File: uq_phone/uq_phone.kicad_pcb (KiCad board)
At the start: 4 copper layers, 116.9 x 105 mm, 169 parts, among them J1 USB4105-GF-A, J10 Conn_01x02, J11 FTSH-105-XX-X-DV, J2 S3B-PH-SM4-TB_LF__SN_, J3 20279-001E-03, J4 20279-001E-03, J5 KP15B-6S-SF_800_, J7 Conn_01x02, J8 541324562, J9 SJ-3551B-MSMT-TR-67, Q1 MMBT3904, Q2 MMBT3904, U1 MCP73871-2CCI_ML, U10 TS3A5018RSVR, U11 NAU88C22YG, U12 MCP1664T-E/OT, U13 TPD3F303DQDR, U14 TPD8F003DQDR, U2 TPS62162DSGR, U3 BQ27441DRZR-G1A, U4 RC7620_1104625, U5 TXB0108RGYR, U6 TXB0108RGYR, U7 STM32H730VBTx, U8 LSM6DSVTR, U9 DRV2603RUNR

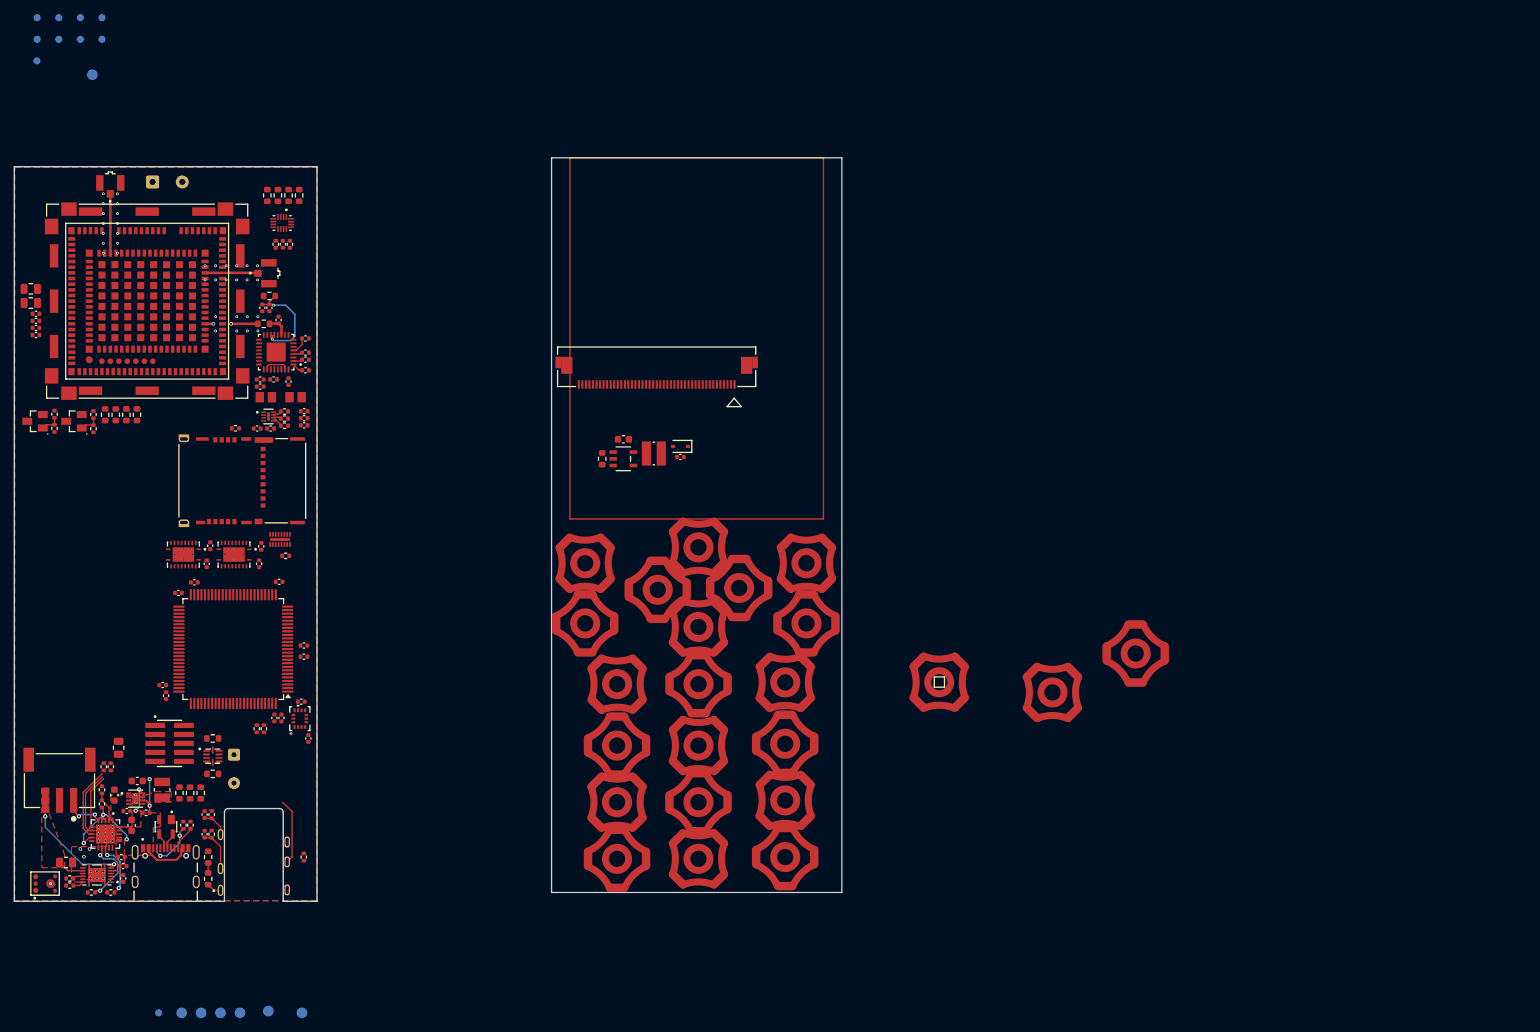
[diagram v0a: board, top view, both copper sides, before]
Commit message: Add LEDs, Inital Buttons
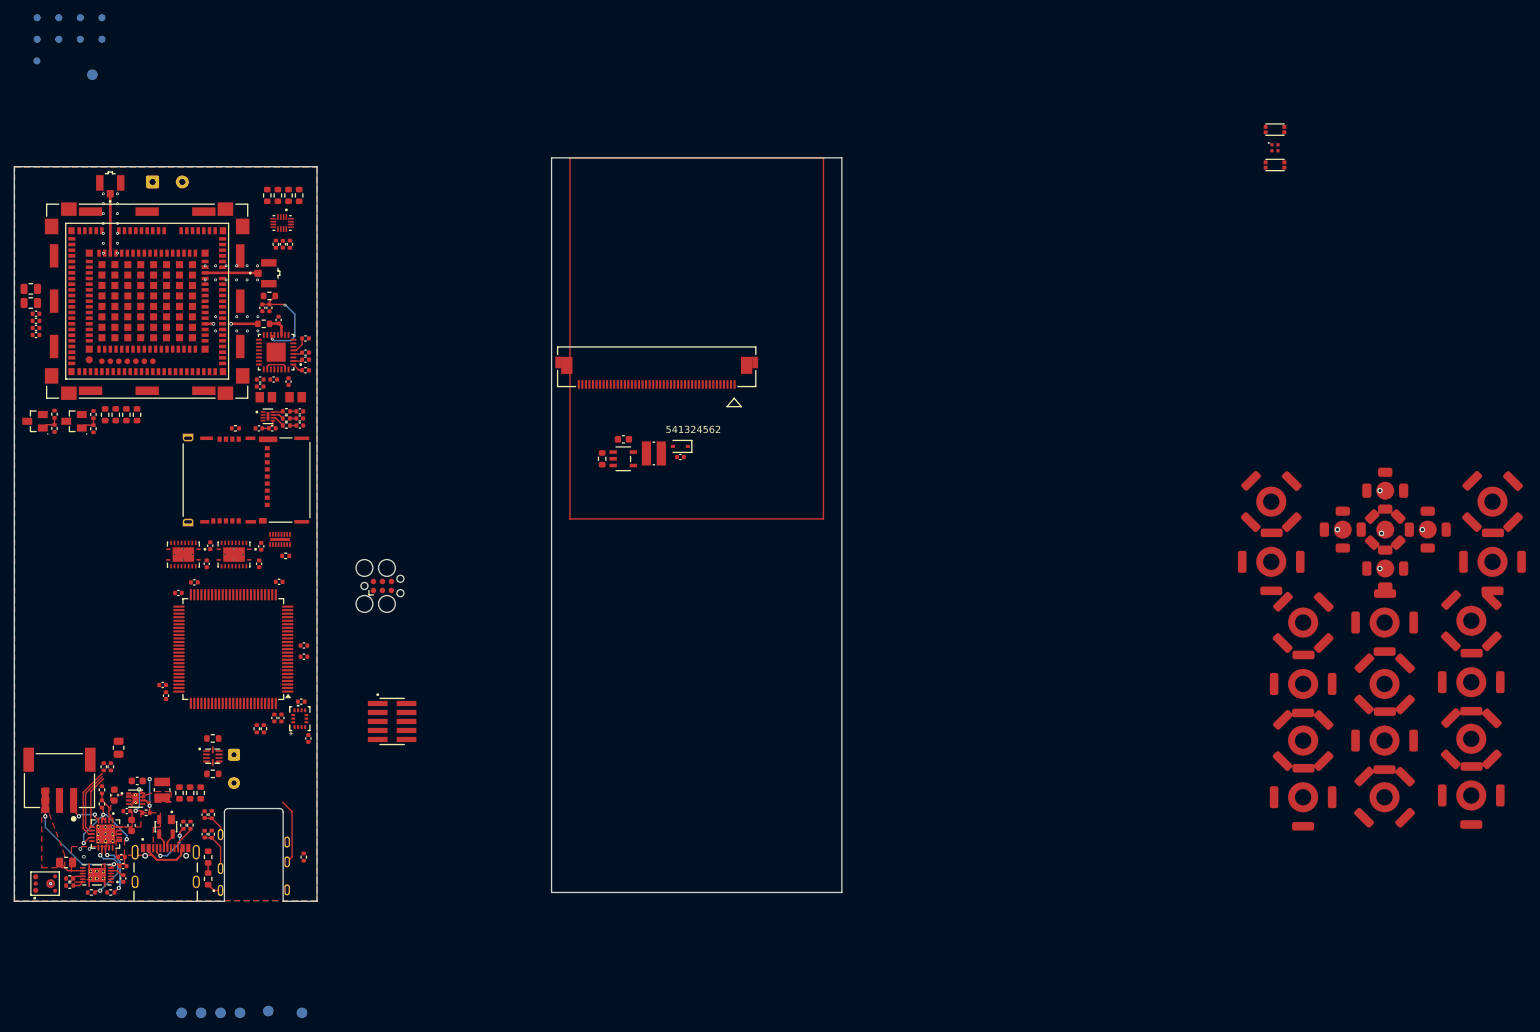
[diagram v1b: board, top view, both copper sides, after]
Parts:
- removed the REF** at (124.0, 133.2)
- removed the REF** at (118.2, 128.0)
- removed the REF** at (124.0, 122.0)
- removed the REF** at (185.8, 137.0)
- removed the REF** at (158.0, 141.1)
- removed the REF** at (174.0, 142.5)
- removed the REF** at (129.8, 127.8)
- removed TP19: TestPoint, TestPoint:TestPoint_Pad_D1.0mm
- removed U13: TPD3F303DQDR, TPD3F303DQDR:SON40P170X135X80-9N
- added J12: Conn_ARM_SWD_TagConnect_TC2030, Connector:Tag-Connect_TC2030-IDC-FP_2x03_P1.27mm_Vertical, F.Cu at (79.4, 127.5)
- added LED1: XINGLIGHT XL-1010RGBC-WS2812B, custom_footprints:XL-1010RGBC-WS2812B, F.Cu at (205.0, 65.2)
- added REF**: 6mmSnaptron, custom_footprints:6mmSnaptron, F.Cu at (215.0, 119.5)
- added REF**: 6mmSnaptron, custom_footprints:6mmSnaptron, F.Cu at (221.0, 114.0)
- added REF**: 6mmSnaptron, custom_footprints:6mmSnaptron, F.Cu at (221.0, 119.5)
- added REF**: 6mmSnaptron, custom_footprints:6mmSnaptron, F.Cu at (227.0, 119.5)
- added REF**: 6mmSnaptron, custom_footprints:6mmSnaptron, F.Cu at (221.0, 125.0)
- added SW1: SKTAAAE010, custom_footprints:SKTAAAE010, F.Cu at (204.1, 62.6)
- added SW2: SKTAAAE010, custom_footprints:SKTAAAE010, F.Cu at (204.1, 67.6)
- added U10: TPD3F303DQDR, TPD3F303DQDR:SON40P170X135X80-9N, F.Cu at (63.2, 103.5)
- moved REF** 97.3 mm to (236.2, 115.5)
- moved REF** 97.3 mm to (209.4, 149.3)
- moved REF** 97.3 mm to (209.4, 157.3)
- moved REF** 97.3 mm to (209.4, 141.3)
- moved REF** 97.3 mm to (220.9, 149.3)
- moved REF** 97.3 mm to (204.9, 124.0)
- moved REF** 97.3 mm to (204.9, 115.5)
- moved REF** 97.3 mm to (220.9, 157.3)
- moved REF** 97.3 mm to (220.9, 141.3)
- moved REF** 97.3 mm to (233.2, 157.1)
- moved REF** 97.3 mm to (233.2, 141.1)
- moved REF** 97.3 mm to (236.2, 124.0)
- moved REF** 97.3 mm to (233.2, 149.1)
- moved REF** 97.3 mm to (209.4, 132.6)
- moved REF** 97.3 mm to (220.9, 132.6)
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- renumbered C34 to C50, C46 to C56, MK1 to MK2, U10 to U15, U11 to U16
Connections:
- C39 pad 1: Net-(U11-RMICN) -> unconnected-(C39-Pad1)
- C44 pad 1: Net-(U11-VREF) -> unconnected-(C44-Pad1)
- C56 pad 1: Net-(MK1-OUTPUT) -> (no net)
- MK2 pad 1: Net-(MK1-OUTPUT) -> (no net)
- R41 pad 2: Net-(U10-~{EN}) -> unconnected-(R41-Pad2)
- U15 pad 13: Net-(U10-~{EN}) -> unconnected-(R41-Pad2)
- U16 pad 19: unconnected-(U11-LAUXIN-Pad19) -> (no net)
- U16 pad 20: unconnected-(U11-RAUXIN-Pad20) -> (no net)
- U16 pad 21: unconnected-(U11-AUXOUT1-Pad21) -> (no net)
- U16 pad 22: unconnected-(U11-AUXOUT2-Pad22) -> (no net)
- U16 pad 27: Net-(U11-VREF) -> unconnected-(C44-Pad1)
- U16 pad 3: unconnected-(U11-LLIN/GPIO2-Pad3) -> (no net)
- U16 pad 5: Net-(U11-RMICN) -> unconnected-(C39-Pad1)
- U16 pad 6: unconnected-(U11-RLIN/GPIO3-Pad6) -> (no net)
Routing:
- net unconnected-(C39-Pad1): track 0.00 -> 2.44 mm
- net Net-(U11-RMICN): track 2.44 -> 0.00 mm
- net SIM_VDD: track 0.00 -> 2.26 mm
- net SIM_RST: track 0.00 -> 0.91 mm
- net SIM_DATA: track 0.00 -> 0.91 mm
- net SIM_CLK: track 0.00 -> 0.90 mm

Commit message: Routing Init
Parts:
- removed the J11 at (80.7, 146.6)
- removed the REF** at (209.4, 132.6)
- removed the REF** at (236.2, 115.5)
- removed the REF** at (209.4, 149.3)
- removed the REF** at (209.4, 157.3)
- removed the REF** at (209.4, 141.3)
- removed the REF** at (220.9, 149.3)
- removed the REF** at (204.9, 124.0)
- removed the REF** at (215.0, 119.5)
- removed the REF** at (221.0, 114.0)
- removed the REF** at (204.9, 115.5)
- removed the REF** at (220.9, 157.3)
- removed the REF** at (220.9, 141.3)
- removed the REF** at (221.0, 119.5)
- removed the REF** at (233.2, 157.1)
- removed the REF** at (227.0, 119.5)
- removed the REF** at (220.9, 132.6)
- removed the REF** at (233.2, 141.1)
- removed the REF** at (233.2, 132.4)
- removed the REF** at (236.2, 124.0)
- removed the REF** at (233.2, 149.1)
- removed the REF** at (221.0, 125.0)
- removed SW1, SW2: SKTAAAE010, custom_footprints:SKTAAAE010
- added LED10: XL-1010RGBC, custom_footprints:XL-1010RGBC-WS2812B, F.Cu at (115.4, 139.4)
- added LED11: XL-1010RGBC, custom_footprints:XL-1010RGBC-WS2812B, F.Cu at (115.4, 141.9)
- added LED12: XL-1010RGBC, custom_footprints:XL-1010RGBC-WS2812B, F.Cu at (115.4, 144.5)
- added LED13: XL-1010RGBC, custom_footprints:XL-1010RGBC-WS2812B, F.Cu at (118.2, 131.8)
- added LED14: XL-1010RGBC, custom_footprints:XL-1010RGBC-WS2812B, F.Cu at (118.2, 134.4)
- added LED15: XL-1010RGBC, custom_footprints:XL-1010RGBC-WS2812B, F.Cu at (118.2, 136.9)
- added LED16: XL-1010RGBC, custom_footprints:XL-1010RGBC-WS2812B, F.Cu at (118.2, 139.4)
- added LED17: XL-1010RGBC, custom_footprints:XL-1010RGBC-WS2812B, F.Cu at (118.2, 141.9)
- added LED2: XL-1010RGBC, custom_footprints:XL-1010RGBC-WS2812B, F.Cu at (112.7, 134.4)
- added LED3: XL-1010RGBC, custom_footprints:XL-1010RGBC-WS2812B, F.Cu at (112.7, 136.9)
- added LED4: XL-1010RGBC, custom_footprints:XL-1010RGBC-WS2812B, F.Cu at (112.7, 139.4)
- added LED5: XL-1010RGBC, custom_footprints:XL-1010RGBC-WS2812B, F.Cu at (112.7, 141.9)
- added LED6: XL-1010RGBC, custom_footprints:XL-1010RGBC-WS2812B, F.Cu at (112.7, 144.5)
- added LED7: XL-1010RGBC, custom_footprints:XL-1010RGBC-WS2812B, F.Cu at (115.4, 131.8)
- added LED8: XL-1010RGBC, custom_footprints:XL-1010RGBC-WS2812B, F.Cu at (115.4, 134.4)
- added LED9: XL-1010RGBC, custom_footprints:XL-1010RGBC-WS2812B, F.Cu at (115.4, 136.9)
- added R48: 330R, Resistor_SMD:R_0402_1005Metric, F.Cu at (108.8, 145.3)
- added REF**: 8.5mmSnaptron, custom_footprints:8.5mmSnaptron, F.Cu at (220.4, 151.7)
- added REF**: 8.5mmSnaptron, custom_footprints:8.5mmSnaptron, F.Cu at (232.7, 159.4)
- added REF**: 8.5mmSnaptron, custom_footprints:8.5mmSnaptron, F.Cu at (235.7, 118.0)
- added REF**: 8.5mmSnaptron, custom_footprints:8.5mmSnaptron, F.Cu at (232.7, 143.4)
- added REF**: 8.5mmSnaptron, custom_footprints:8.5mmSnaptron, F.Cu at (208.9, 151.7)
- added REF**: 8.5mmSnaptron, custom_footprints:8.5mmSnaptron, F.Cu at (204.4, 118.0)
- added REF**: 8.5mmSnaptron, custom_footprints:8.5mmSnaptron, F.Cu at (232.7, 151.4)
- added REF**: 6mmSnaptron, custom_footprints:6mmSnaptron, F.Cu at (220.5, 127.4)
- added REF**: 8.5mmSnaptron, custom_footprints:8.5mmSnaptron, F.Cu at (220.4, 135.0)
- added REF**: 6mmSnaptron, custom_footprints:6mmSnaptron, F.Cu at (226.5, 121.9)
- added REF**: 6mmSnaptron, custom_footprints:6mmSnaptron, F.Cu at (214.5, 121.9)
- added REF**: 8.5mmSnaptron, custom_footprints:8.5mmSnaptron, F.Cu at (204.4, 126.5)
- added REF**: 6mmSnaptron, custom_footprints:6mmSnaptron, F.Cu at (220.5, 116.4)
- added REF**: 8.5mmSnaptron, custom_footprints:8.5mmSnaptron, F.Cu at (208.9, 135.0)
- added REF**: 8.5mmSnaptron, custom_footprints:8.5mmSnaptron, F.Cu at (220.4, 159.7)
- added REF**: 6mmSnaptron, custom_footprints:6mmSnaptron, F.Cu at (220.5, 121.9)
- added REF**: 8.5mmSnaptron, custom_footprints:8.5mmSnaptron, F.Cu at (220.4, 143.7)
- added REF**: 8.5mmSnaptron, custom_footprints:8.5mmSnaptron, F.Cu at (232.7, 134.8)
- added REF**: 8.5mmSnaptron, custom_footprints:8.5mmSnaptron, F.Cu at (208.9, 143.7)
- added REF**: 8.5mmSnaptron, custom_footprints:8.5mmSnaptron, F.Cu at (208.9, 159.7)
- added REF**: 8.5mmSnaptron, custom_footprints:8.5mmSnaptron, F.Cu at (235.7, 126.5)
- LED1: value XINGLIGHT XL-1010RGBC-WS2812B -> XL-1010RGBC
- Q1, Q2: value MMBT3904 -> MMBT3904LP-7; footprint MMBT3904LT1G:SOT95P240X111-3N -> MMBT3904LP-7:DFN101X61X53-3N
- moved LED1 113.9 mm to (112.7, 131.8)
- moved TP6 111.9 mm to (29.7, 82.6)
- moved C27 51.0 mm to (49.2, 102.0), turned to 180 degrees
- moved C28 46.6 mm to (47.4, 102.0), turned to 0 degrees
- moved TP10 46.5 mm to (40.2, 93.5)
- moved U8 46.4 mm to (48.3, 104.1), turned to 180 degrees
- moved R45 46.3 mm to (61.7, 119.9), turned to 180 degrees
- moved TP12 44.8 mm to (42.3, 93.5)
- moved TP11 44.5 mm to (41.2, 91.7)
- moved TP14 44.0 mm to (44.3, 93.5)
- moved TP16 43.3 mm to (46.4, 93.6)
- moved TP2 42.7 mm to (28.8, 157.8)
- moved TP13 42.6 mm to (43.4, 91.8)
- moved TP15 42.0 mm to (45.4, 91.8)
- moved TP9 40.3 mm to (35.7, 87.4)
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- renumbered C15 to C10, C16 to C11, C17 to C12, C18 to C13, C19 to C14, C20 to C15, C21 to C16, C22 to C17, C23 to C18, C24 to C19, C25 to C20, C26 to C21, C27 to C22, C28 to C23, C29 to C24, C30 to C25, C31 to C26, C32 to C27, C33 to C28, C8 to C29, C9 to C30, C10 to C31, C11 to C32, C12 to C33, C48 to C34, C49 to C35, C50 to C36, C35 to C37, C36 to C38, C37 to C39, C38 to C40, C39 to C41, C56 to C42, C47 to C43, C40 to C44, C41 to C45, C42 to C46, C43 to C47, C44 to C48, C45 to C49, C7 to C6, C6 to C7, C13 to C8, C14 to C9, D5 to D2, J9 to J10, J10 to J11, J12 to J6, J5 to J8, J8 to J9, MK2 to MK1, R8 to R10, R39 to R23, R26 to R24, R27 to R25, R28 to R26, R29 to R27, R30 to R28, R31 to R29, R23 to R30, R24 to R31, R25 to R32, R32 to R33, R38 to R34, R40 to R35, R41 to R36, R42 to R37, R47 to R38, R48 to R39, R43 to R40, R44 to R41, R45 to R42, R46 to R43, R49 to R44, R50 to R45, R51 to R46, R54 to R47, R9 to R8, R10 to R9, U14 to U11, U15 to U13, U16 to U14
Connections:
- C41 pad 1: unconnected-(C39-Pad1) -> Net-(U14-RMICN)
- C42 pad 1: (no net) -> Net-(MK1-OUTPUT)
- C48 pad 1: unconnected-(C44-Pad1) -> Net-(U14-VREF)
- D1 pad 3: USB_P -> USB_N
- D1 pad 4: USB_N -> USB_P
- LED1 pad 1: unconnected-(LED1-DO-Pad1) -> Net-(LED1-DO)
- LED1 pad 2: unconnected-(LED1-VDD-Pad2) -> +3.3V
- LED1 pad 3: unconnected-(LED1-GND-Pad3) -> GND
- LED1 pad 4: unconnected-(LED1-DI-Pad4) -> Net-(LED1-DI)
- MK1 pad 1: (no net) -> Net-(MK1-OUTPUT)
- R35 pad 1: AUD_SW -> AUD_SW_L
- R36 pad 2: unconnected-(R41-Pad2) -> Net-(U13-~{EN})
- U13 pad 13: unconnected-(R41-Pad2) -> Net-(U13-~{EN})
- U13 pad 15: AUD_SW -> AUD_SW_L
- U13 pad 9: MCU_AUD_IN -> unconnected-(U13-NC3-Pad9)
- U14 pad 19: (no net) -> unconnected-(U14-LAUXIN-Pad19)
- U14 pad 20: (no net) -> unconnected-(U14-RAUXIN-Pad20)
- U14 pad 21: (no net) -> unconnected-(U14-AUXOUT1-Pad21)
- U14 pad 22: (no net) -> unconnected-(U14-AUXOUT2-Pad22)
- U14 pad 27: unconnected-(C44-Pad1) -> Net-(U14-VREF)
- U14 pad 3: (no net) -> unconnected-(U14-LLIN/GPIO2-Pad3)
- U14 pad 5: unconnected-(C39-Pad1) -> Net-(U14-RMICN)
- U14 pad 6: (no net) -> unconnected-(U14-RLIN/GPIO3-Pad6)
- U4 pad 38: MOB_GNSS_ANT -> unconnected-(U4A-RF_GNSS-Pad38)
- U4 pad P1: (no net) -> GND
- U4 pad P10: (no net) -> GND
- U4 pad P11: (no net) -> GND
- U4 pad P12: (no net) -> GND
- U4 pad P13: (no net) -> GND
- U4 pad P14: (no net) -> GND
- U4 pad P15: (no net) -> GND
- U4 pad P16: (no net) -> GND
- U4 pad P17: (no net) -> GND
- U4 pad P18: (no net) -> GND
- U4 pad P19: (no net) -> GND
- U4 pad P2: (no net) -> GND
- U4 pad P20: (no net) -> GND
- U4 pad P3: (no net) -> GND
- U4 pad P4: (no net) -> GND
- U4 pad P5: (no net) -> GND
- U4 pad P6: (no net) -> GND
- U4 pad P7: (no net) -> GND
- U4 pad P8: (no net) -> GND
- U4 pad P9: (no net) -> GND
- U5 pad 1: MOB_DTR -> MOB_DSR
- U5 pad 12: MCU_DSR -> MCU_RI
- U5 pad 16: MCU_RI -> MCU_RXD
- U5 pad 17: MCU_DCD -> MCU_DTR
- U5 pad 18: MCU_RXD -> MCU_DCD
- U5 pad 20: MCU_DTR -> MCU_DSR
- U5 pad 3: MOB_RXD -> MOB_DCD
- U5 pad 4: MOB_DCD -> MOB_DTR
- U5 pad 5: MOB_RI -> MOB_RXD
- U5 pad 9: MOB_DSR -> MOB_RI
- U6 pad 12: AUD_SW_H -> MCU_AUD_OUT_L_H
- U6 pad 13: MCU_AUD_SYNC_H -> MCU_AUD_BCLK_H
- U6 pad 14: MCU_AUD_BCLK_H -> AUD_SW_H
- U6 pad 15: MCU_AUD_OUT_L_H -> MCU_AUD_SYNC_H
- U6 pad 6: MCU_AUD_OUT_L -> MCU_AUD_SYNC_L
- U6 pad 7: MCU_AUD_BCLK_L -> AUD_SW_L
- U6 pad 8: MCU_AUD_SYNC_L -> MCU_AUD_BCLK_L
- U6 pad 9: AUD_SW_L -> MCU_AUD_OUT_L
- U7 pad 35: unconnected-(U7-PB1-Pad35) -> MOB_WAKE_H
- U7 pad 36: unconnected-(U7-PB2-Pad36) -> MOB_PWR_CTL
- U7 pad 47: unconnected-(U7-PB11-Pad47) -> MOB_RST_CTL
- U7 pad 59: MCU_DTR -> MCU_DCD
- U7 pad 60: MCU_DCD -> MCU_DTR
- U7 pad 91: MOB_RST_CTL -> unconnected-(U7-PB5-Pad91)
- U7 pad 92: MOB_WAKE_H -> unconnected-(U7-PB6-Pad92)
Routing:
- net +1.8V: track 0.00 -> 112.0 mm, vias 0 -> 6
- net Net-(MK1-OUTPUT): track 0.00 -> 110.4 mm, vias 0 -> 2
- net +3.3V: track 6.14 -> 111.2 mm, vias 2 -> 7
- net AGND: track 0.00 -> 99.7 mm, vias 0 -> 3
- net HP_DET: track 9.27 -> 90.3 mm, vias 0 -> 5
- net Net-(C37-Pad2): track 1.43 -> 81.5 mm, vias 0 -> 2
- net +VMOB: track 0.00 -> 80.0 mm, vias 0 -> 1
- net SDA: track 0.00 -> 64.0 mm, vias 0 -> 4
- net SCL: track 0.00 -> 63.4 mm, vias 0 -> 4
- net Net-(U4A-USB_VBUS): track 0.00 -> 63.0 mm, vias 0 -> 2
- net /Mobile/MOB_USB_N: track 0.00 -> 63.0 mm, vias 0 -> 2
- net /Mobile/MOB_USB_P: track 0.00 -> 62.9 mm, vias 0 -> 2
- net FUEL_GPO: track 1.56 -> 56.6 mm, vias 0 -> 3
- net MCU_AUD_SYNC_L: track 0.00 -> 53.1 mm, vias 0 -> 2
- net MCU_AUD_BCLK_L: track 0.00 -> 53.1 mm, vias 0 -> 2
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- added copper zone on F.Cu, net +VMOB
- added copper zone on B.Cu, net AGND
- added copper zone on F.Cu, net AGND
- added copper zone on In2.Cu, net GND

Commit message: Update routing
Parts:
- removed REF** (x16): 8.5mmSnaptron, custom_footprints:8.5mmSnaptron
- removed REF** (x5): 6mmSnaptron, custom_footprints:6mmSnaptron
- added M1: VCDM0834B004L, custom_footprints:Motor_8mm, F.Cu at (64.8, 153.0)
- J7: footprint Connector_Wire:SolderWire-0.15sqmm_1x02_P4mm_D0.5mm_OD1.5mm -> Connector_Wire:SolderWire-0.1sqmm_1x02_P3.6mm_D0.4mm_OD1mm
- moved TP7 41.6 mm to (65.8, 86.6)
- moved R29 32.5 mm to (51.0, 152.6)
- moved R28 32.5 mm to (53.4, 153.4)
- moved U9 32.5 mm to (53.4, 150.9)
- moved J7 32.0 mm to (56.6, 151.4)
- moved TP3 30.3 mm to (28.8, 154.4)
- moved L2 23.0 mm to (82.4, 149.0)
- moved U12 22.9 mm to (78.1, 148.8)
- moved C35 18.8 mm to (86.5, 145.8)
- moved D2 18.8 mm to (86.5, 144.3)
- moved R34 18.8 mm to (75.8, 144.8)
- moved C34 18.8 mm to (78.7, 142.1)
- moved J9 6.61 mm to (123.0, 100.9), turned to 0 degrees
- moved J6 5.69 mm to (44.4, 145.7), turned to -90 degrees
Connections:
- U8 pad 4: IMU_INT1 -> unconnected-(U8-INT1-Pad4)
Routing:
- net +3.3V: track 111.2 -> 227.3 mm, vias 7 -> 14
- net MIC_BIAS: track 29.7 -> 107.9 mm
- net HP_RIGHT: track 2.04 -> 78.9 mm, vias 1 -> 2
- net HP_LEFT: track 2.28 -> 76.2 mm, vias 1 -> 2
- net RST: track 1.83 -> 37.6 mm, vias 0 -> 2
- net AUD_SDA: track 1.50 -> 35.4 mm, vias 2 -> 3
- net GND: track 5.86 -> 35.7 mm, vias 172 -> 174
- net VIB_PWM: track 0.00 -> 28.8 mm, vias 0 -> 2
- net SCL: track 63.4 -> 91.9 mm, vias 4 -> 6
- net SDA: track 64.0 -> 91.4 mm, vias 4 -> 6
- net VIB_EN: track 0.00 -> 26.0 mm, vias 0 -> 2
- net SWCLK: track 0.00 -> 8.66 mm
- net SWDIO: track 0.00 -> 8.64 mm
- net AGND: track 99.7 -> 106.8 mm
- net Net-(J7-Pin_2): track 0.00 -> 6.13 mm
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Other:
- board text removed: "1.3mm spacing on vias"
- board text removed: "Calcs made for JLC04101H-7628(Standard/Finished thickness1.02mm±10%)"

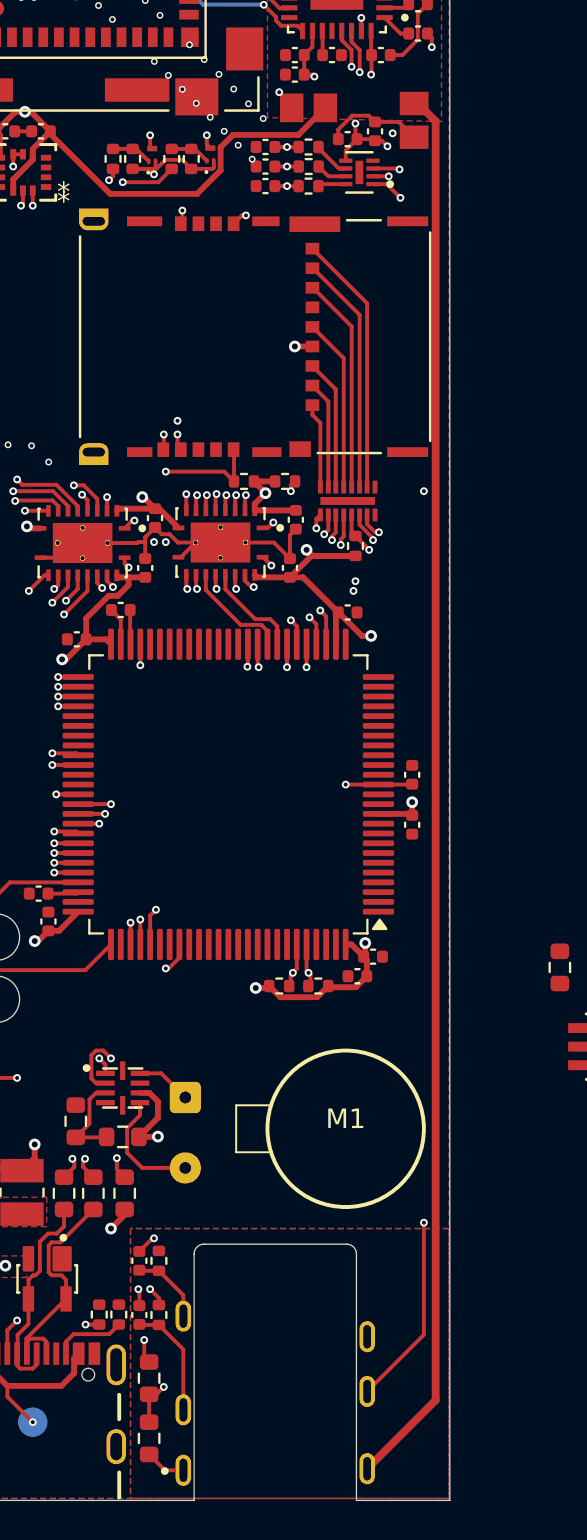
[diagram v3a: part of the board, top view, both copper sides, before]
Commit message: Update to Kicad 9.0, Add 3d Models
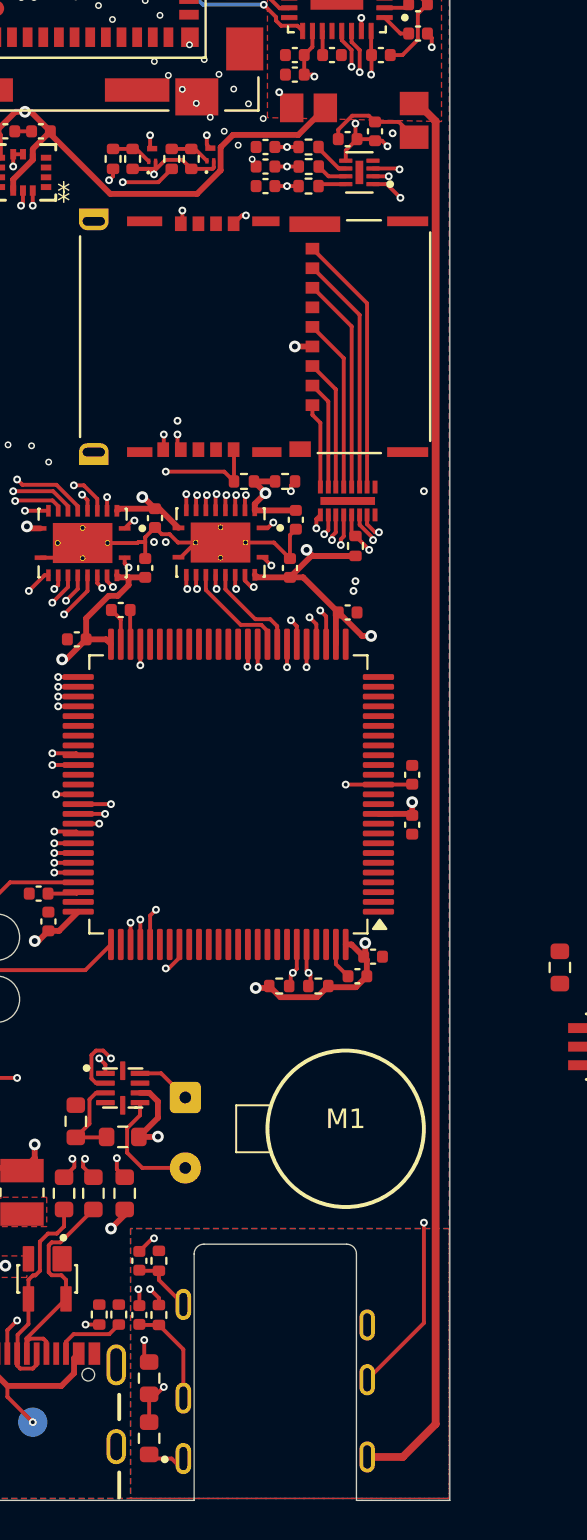
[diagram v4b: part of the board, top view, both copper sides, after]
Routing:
- net GND: track 35.7 -> 37.6 mm
